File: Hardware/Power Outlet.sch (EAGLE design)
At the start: 37 parts, among them IC1 ATMega 328p-pu, IC2 ULN2003AD, K1 G5LE, K2 G5LE, Q1 16MHz, X1 VIN, X2 VOUT2, X3 VOUT1, X7 EARTH

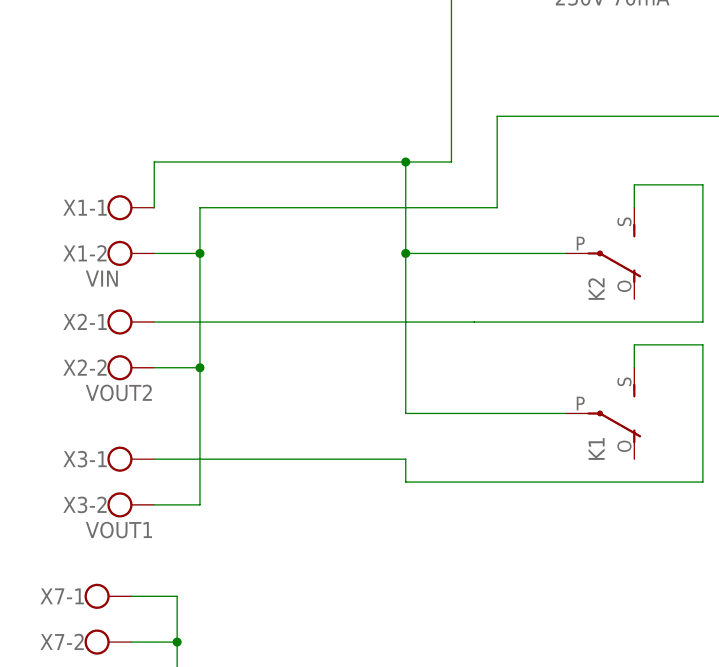
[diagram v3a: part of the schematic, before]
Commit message: updated Fuse Holder for part that is in stock. Updated wrong Processor footprint also fixed screw terminals wrong way round
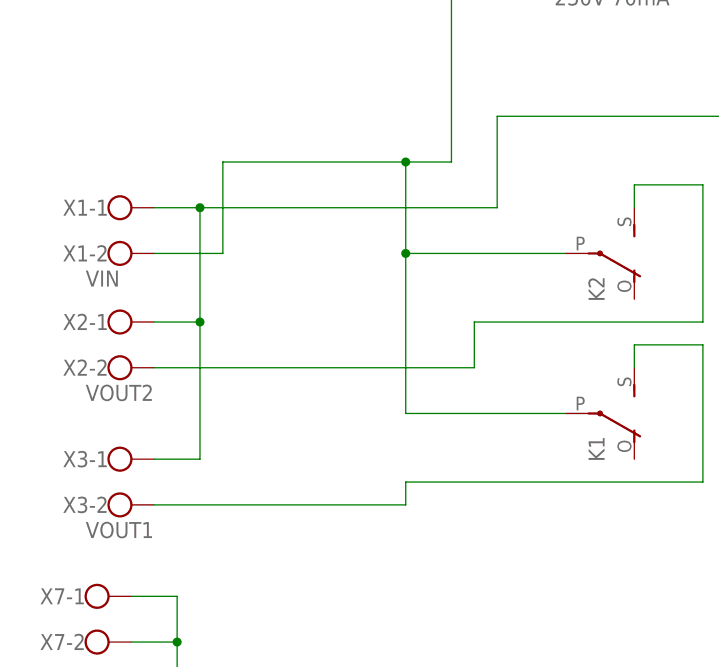
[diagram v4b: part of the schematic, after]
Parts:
- F1: device fuse:GSH15 -> fuse:FUSESH22,5A
- IC1: device ic-package:DIL28-4 -> ic-package:DIL28-3
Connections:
- net N$1: now also X1-2.KL; no longer X1-1.KL
- net N$11: now also X2-2.KL; no longer X2-1.KL
- net N$14: now also X3-2.KL; no longer X3-1.KL
- net N$3: now also X1-1.KL, X2-1.KL, X3-1.KL; no longer X1-2.KL, X2-2.KL, X3-2.KL
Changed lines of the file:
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@@
 <parts>
 <part name="U$1" library="VTX214001103" deviceset="VTX-214-001-103" device=""/>
-<part name="F1" library="fuse" deviceset="GSH15" device="" value="230V 70mA"/>
+<part name="F1" library="fuse" deviceset="FUSE" device="SH22,5A" value="230V 70mA"/>
 <part name="R1" library="varistor" deviceset="P594" device=""/>
 <part name="C1" library="rcl" deviceset="CPOL-EU" device="E2,5-6E" value="10u"/>
@@
 <part name="LED1" library="led" deviceset="LED" device="5MM" value="OUT2"/>
 <part name="LED2" library="led" deviceset="LED" device="5MM" value="OUT1"/>
-<part name="IC1" library="ic-package" deviceset="DIL28" device="-4" value="ATMega 328p-pu"/>
+<part name="IC1" library="ic-package" deviceset="DIL28" device="-3" value="ATMega 328p-pu"/>
 <part name="Q1" library="crystal" deviceset="CRYSTAL" device="HC49S" value="16MHz"/>
 <part name="R2" library="rcl" deviceset="R-EU_" device="R1206W" value="10k"/>
@@
 <instances>
 <instance part="U$1" gate="G$1" x="33.02" y="68.58"/>
-<instance part="F1" gate="1" x="-25.4" y="76.2"/>
+<instance part="F1" gate="G$1" x="-25.4" y="76.2"/>
 <instance part="R1" gate="1" x="-2.54" y="68.58" rot="R90"/>
 <instance part="C1" gate="G$1" x="53.34" y="68.58"/>
@@
 <net name="N$2" class="0">
 <segment>
-<pinref part="F1" gate="1" pin="2"/>
+<pinref part="F1" gate="G$1" pin="2"/>
 <wire x1="-20.32" y1="76.2" x2="-2.54" y2="76.2" width="0.1524" layer="91"/>
 <pinref part="U$1" gate="G$1" pin="LIVE"/>
@@
 <wire x1="-35.56" y1="60.96" x2="-2.54" y2="60.96" width="0.1524" layer="91"/>
 <junction x="-2.54" y="60.96"/>
-<pinref part="X3" gate="-2" pin="KL"/>
-<wire x1="-73.66" y1="17.78" x2="-68.58" y2="17.78" width="0.1524" layer="91"/>
-<pinref part="X2" gate="-2" pin="KL"/>
-<wire x1="-73.66" y1="33.02" x2="-68.58" y2="33.02" width="0.1524" layer="91"/>
-<wire x1="-68.58" y1="33.02" x2="-68.58" y2="17.78" width="0.1524" layer="91"/>
-<pinref part="X1" gate="-2" pin="KL"/>
-<wire x1="-73.66" y1="45.72" x2="-68.58" y2="45.72" width="0.1524" layer="91"/>
-<wire x1="-68.58" y1="45.72" x2="-68.58" y2="33.02" width="0.1524" layer="91"/>
-<junction x="-68.58" y="33.02"/>
-<wire x1="-68.58" y1="45.72" x2="-68.58" y2="50.8" width="0.1524" layer="91"/>
-<junction x="-68.58" y="45.72"/>
+<wire x1="-68.58" y1="50.8" x2="-68.58" y2="38.1" width="0.1524" layer="91"/>
+<wire x1="-68.58" y1="38.1" x2="-68.58" y2="22.86" width="0.1524" layer="91"/>
+<pinref part="X3" gate="-1" pin="KL"/>
+<wire x1="-68.58" y1="22.86" x2="-73.66" y2="22.86" width="0.1524" layer="91"/>
+<junction x="-68.58" y="38.1"/>
+<pinref part="X2" gate="-1" pin="KL"/>
+<wire x1="-73.66" y1="38.1" x2="-68.58" y2="38.1" width="0.1524" layer="91"/>
+<pinref part="X1" gate="-1" pin="KL"/>
+<wire x1="-73.66" y1="50.8" x2="-68.58" y2="50.8" width="0.1524" layer="91"/>
+<junction x="-68.58" y="50.8"/>
 </segment>
 </net>
@@
 <net name="N$1" class="0">
 <segment>
-<pinref part="F1" gate="1" pin="1"/>
+<pinref part="F1" gate="G$1" pin="1"/>
 <wire x1="-30.48" y1="76.2" x2="-40.64" y2="76.2" width="0.1524" layer="91"/>
 <wire x1="-40.64" y1="76.2" x2="-40.64" y2="55.88" width="0.1524" layer="91"/>
@@
 <junction x="-45.72" y="45.72"/>
 <junction x="-45.72" y="55.88"/>
-<pinref part="X1" gate="-1" pin="KL"/>
-<wire x1="-73.66" y1="50.8" x2="-73.66" y2="55.88" width="0.1524" layer="91"/>
-<wire x1="-73.66" y1="55.88" x2="-45.72" y2="55.88" width="0.1524" layer="91"/>
+<pinref part="X1" gate="-2" pin="KL"/>
+<wire x1="-66.04" y1="55.88" x2="-45.72" y2="55.88" width="0.1524" layer="91"/>
+<wire x1="-73.66" y1="45.72" x2="-66.04" y2="45.72" width="0.1524" layer="91"/>
+<wire x1="-66.04" y1="45.72" x2="-66.04" y2="55.88" width="0.1524" layer="91"/>
 </segment>
 </net>
@@
 <wire x1="-12.7" y1="53.34" x2="-12.7" y2="38.1" width="0.1524" layer="91"/>
 <wire x1="-12.7" y1="38.1" x2="-38.1" y2="38.1" width="0.1524" layer="91"/>
-<pinref part="X2" gate="-1" pin="KL"/>
-<wire x1="-73.66" y1="38.1" x2="-38.1" y2="38.1" width="0.1524" layer="91"/>
+<pinref part="X2" gate="-2" pin="KL"/>
+<wire x1="-73.66" y1="33.02" x2="-38.1" y2="33.02" width="0.1524" layer="91"/>
+<wire x1="-38.1" y1="33.02" x2="-38.1" y2="38.1" width="0.1524" layer="91"/>
 </segment>
 </net>
@@
 <wire x1="-12.7" y1="35.56" x2="-12.7" y2="20.32" width="0.1524" layer="91"/>
 <wire x1="-12.7" y1="20.32" x2="-45.72" y2="20.32" width="0.1524" layer="91"/>
-<wire x1="-45.72" y1="20.32" x2="-45.72" y2="22.86" width="0.1524" layer="91"/>
-<wire x1="-45.72" y1="22.86" x2="-73.66" y2="22.86" width="0.1524" layer="91"/>
-<pinref part="X3" gate="-1" pin="KL"/>
-</segment>
-</net>
+<wire x1="-45.72" y1="20.32" x2="-45.72" y2="17.78" width="0.1524" layer="91"/>
+<pinref part="X3" gate="-2" pin="KL"/>
+<wire x1="-45.72" y1="17.78" x2="-73.66" y2="17.78" width="0.1524" layer="91"/>
+</segment>
+</net>

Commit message: updated to correct componnent values and minor tweaks
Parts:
- C1: value 10u -> 47u
- C5: value 1n -> 0.1u
- Q1: value 16MHz -> 8MHz
- R3, R4: value 330R -> 3k3
- R5, R6, R7, R8: value 10k -> 100R
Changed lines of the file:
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@@
 <part name="F1" library="fuse" deviceset="FUSE" device="SH22,5A" value="230V 70mA"/>
 <part name="R1" library="varistor" deviceset="P594" device=""/>
-<part name="C1" library="rcl" deviceset="CPOL-EU" device="E2,5-6E" value="10u"/>
+<part name="C1" library="rcl" deviceset="CPOL-EU" device="E2,5-6E" value="47u"/>
 <part name="+3V1" library="supply1" deviceset="+3V3" device=""/>
 <part name="GND1" library="supply1" deviceset="GND" device=""/>
@@
 <part name="LED2" library="led" deviceset="LED" device="5MM" value="OUT1"/>
 <part name="IC1" library="ic-package" deviceset="DIL28" device="-3" value="ATMega 328p-pu"/>
-<part name="Q1" library="crystal" deviceset="CRYSTAL" device="HC49S" value="16MHz"/>
+<part name="Q1" library="crystal" deviceset="CRYSTAL" device="HC49S" value="8MHz"/>
 <part name="R2" library="rcl" deviceset="R-EU_" device="R1206W" value="10k"/>
-<part name="R3" library="rcl" deviceset="R-EU_" device="R1206W" value="330R"/>
-<part name="R4" library="rcl" deviceset="R-EU_" device="R1206W" value="330R"/>
+<part name="R3" library="rcl" deviceset="R-EU_" device="R1206W" value="3k3"/>
+<part name="R4" library="rcl" deviceset="R-EU_" device="R1206W" value="3k3"/>
 <part name="C3" library="rcl" deviceset="C-EU" device="C1206K" value="22p"/>
 <part name="C4" library="rcl" deviceset="C-EU" device="C1206K" value="22p"/>
-<part name="C5" library="rcl" deviceset="C-EU" device="C1206K" value="1n"/>
+<part name="C5" library="rcl" deviceset="C-EU" device="C1206K" value="0.1u"/>
 <part name="+3V2" library="supply1" deviceset="+3V3" device=""/>
 <part name="GND2" library="supply1" deviceset="GND" device=""/>
@@
 <part name="SUPPLY1" library="supply2" deviceset="VCC" device=""/>
 <part name="GND8" library="supply1" deviceset="GND" device=""/>
-<part name="R5" library="rcl" deviceset="R-EU_" device="R1206W" value="10k"/>
-<part name="R6" library="rcl" deviceset="R-EU_" device="R1206W" value="10k"/>
+<part name="R5" library="rcl" deviceset="R-EU_" device="R1206W" value="100R"/>
+<part name="R6" library="rcl" deviceset="R-EU_" device="R1206W" value="100R"/>
 <part name="SUPPLY2" library="supply2" deviceset="VCC" device=""/>
 <part name="L1" library="rcl" deviceset="L-EU" device="L3225P"/>
@@
 <part name="SUPPLY4" library="supply2" deviceset="AGND" device=""/>
 <part name="SUPPLY5" library="supply2" deviceset="VCC" device=""/>
-<part name="R7" library="rcl" deviceset="R-EU_" device="R1206W" value="10k"/>
-<part name="R8" library="rcl" deviceset="R-EU_" device="R1206W" value="10k"/>
+<part name="R7" library="rcl" deviceset="R-EU_" device="R1206W" value="100R"/>
+<part name="R8" library="rcl" deviceset="R-EU_" device="R1206W" value="100R"/>
 <part name="X1" library="con-wago-500" deviceset="W237-102" device="" value="VIN"/>
 <part name="X2" library="con-wago-500" deviceset="W237-102" device="" value="VOUT2"/>
